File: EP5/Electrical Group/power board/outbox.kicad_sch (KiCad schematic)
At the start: 18 parts, among them IC3 MCP6C04T-100E_CHY, J1 powertrain1, J1 powertrain2, J1 powertrain3

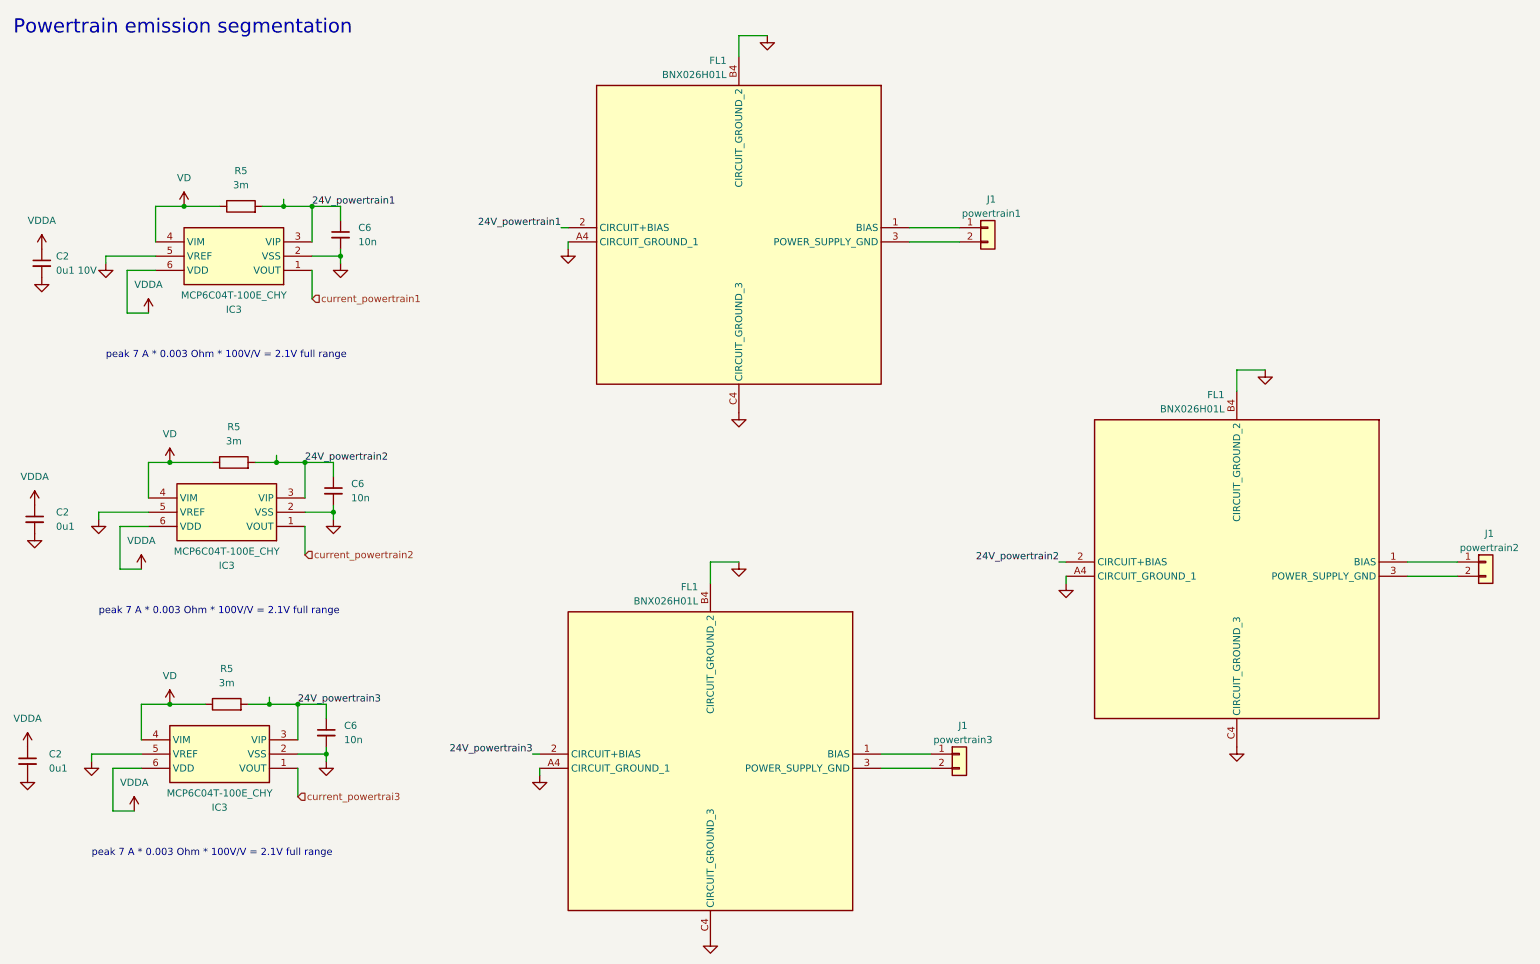
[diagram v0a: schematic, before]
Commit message: update power board for kicad8
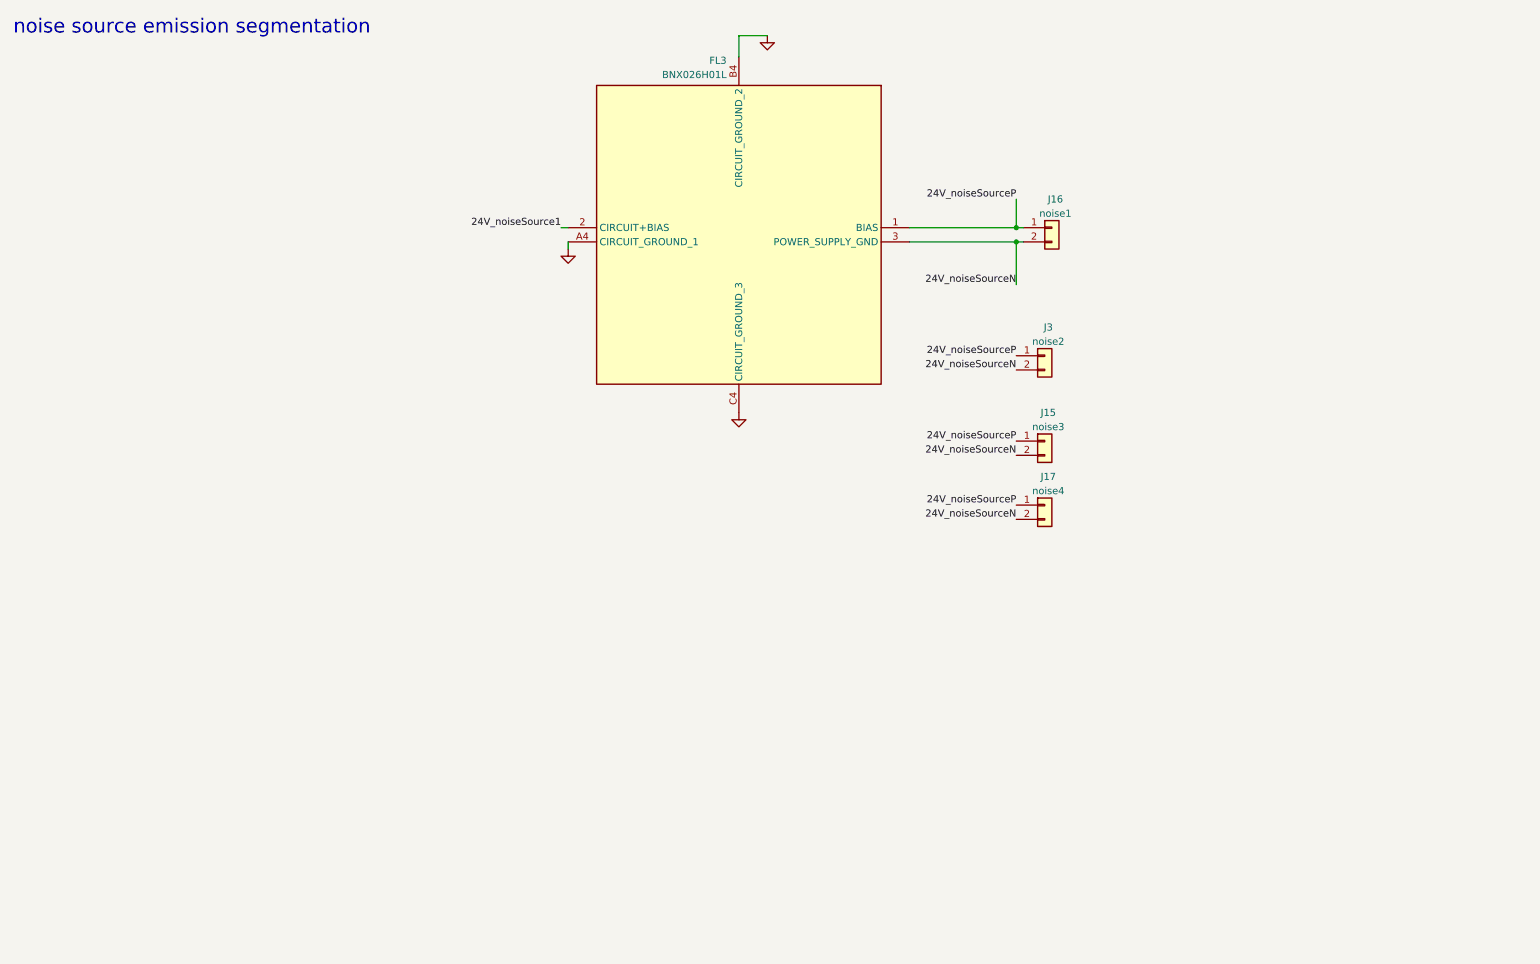
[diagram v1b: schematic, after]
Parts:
- removed C2 (x2): 0u1, Capacitor_SMD:C_0805_2012Metric, symbol Device:C_Small
- removed C2: 0u1 10V, Capacitor_SMD:C_0805_2012Metric, symbol Device:C_Small
- removed C6 (x3): 10n, Capacitor_SMD:C_0805_2012Metric, symbol Device:C_Small
- removed FL1 (x2): BNX026H01L, SamacSys_Parts:BNX024H01K, symbol SamacSys_Parts:BNX026H01L
- removed IC3 (x3): MCP6C04T-100E_CHY, SamacSys_Parts:SOT95P280X145-6N, symbol SamacSys_Parts:MCP6C04T-100E_CHY
- removed J1: powertrain3, Connector_Molex:Molex_KK-396_A-41791-0002_1x02_P3.96mm_Vertical, symbol Connector_Generic:Conn_01x02
- removed J1: powertrain2, Connector_Molex:Molex_KK-396_A-41791-0002_1x02_P3.96mm_Vertical, symbol Connector_Generic:Conn_01x02
- removed R5 (x3): 3m, Resistor_SMD:R_1206_3216Metric, symbol Device:R
- added J15: noise3, Connector_Molex:Molex_KK-396_A-41791-0002_1x02_P3.96mm_Vertical, symbol Connector_Generic:Conn_01x02
- added J17: noise4, Connector_Molex:Molex_KK-396_A-41791-0002_1x02_P3.96mm_Vertical, symbol Connector_Generic:Conn_01x02
- added J3: noise2, Connector_Molex:Molex_KK-396_A-41791-0002_1x02_P3.96mm_Vertical, symbol Connector_Generic:Conn_01x02
- J16: renamed from J1; value powertrain1 -> noise1
- renumbered FL1 to FL3
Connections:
- net 24V_noiseSourceP: now reaches FL3.1 (BIAS), J16.1 (Pin_1)
- net 24V_noiseSourceP: now also J15.1 (Pin_1), J17.1 (Pin_1), J3.1 (Pin_1)
- net 24V_noiseSourceN: now reaches FL3.3 (POWER_SUPPLY_GND), J16.2 (Pin_2)
- net 24V_noiseSourceN: now also J15.2 (Pin_2), J17.2 (Pin_2), J3.2 (Pin_2)
- net 24V_powertrain1 renamed 24V_noiseSource1
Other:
- note added: "noise source emission segmentation"
- note removed: "Powertrain emission segmentation"
- note removed: "peak 7 A * 0.003 Ohm * 100V/V = 2.1V full range"
- moved on the sheet: J16
